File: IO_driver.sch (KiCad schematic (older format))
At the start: 9 parts, among them J2001 BNC, U2001 74LVC2T45DC

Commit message: some fixes; don't recall details :-(
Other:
- moved on the sheet: R2052
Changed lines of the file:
@@
 $Descr A4 11693 8268
 encoding utf-8
-Sheet 11 12
+Sheet 10 12
 Title ""
 Date ""
@@
 	3850 1850 4050 1850
 Connection ~ 4050 1850
-Text HLabel 3250 1850 0    50   BiDi ~ 0
+Text HLabel 2500 1850 0    50   BiDi ~ 0
 DATA
-Wire Wire Line
-	3250 1850 3500 1850
-Text HLabel 3250 2150 0    50   Input ~ 0
+Text HLabel 2500 2150 0    50   Input ~ 0
 DIR
-Wire Wire Line
-	3250 2150 3600 2150
 $Comp
 L Device:C_Small C2001
@@
 L Device:R_Small R?
 U 1 1 60E4921E
-P 3600 2350
+P 3500 2350
 AR Path="/60DC28BD/60E4921E" Ref="R?"  Part="1"
 AR Path="/60E4921E" Ref="R?"  Part="1"
@@
 AR Path="/60E70F2C/60EF9F81/60E4921E" Ref="R2002"  Part="1"
 AR Path="/60E70F2C/60E556C7/60E4921E" Ref="R2052"  Part="1"
-F 0 "R2052" H 3659 2396 50  0000 L CNN
-F 1 "2k2" H 3659 2305 50  0000 L CNN
-F 2 "Resistor_SMD:R_0603_1608Metric" H 3600 2350 50  0001 C CNN
-F 3 "~" H 3600 2350 50  0001 C CNN
-	1    3600 2350
-	1    0    0    -1
-$EndComp
-Wire Wire Line
-	3600 2250 3600 2150
-Connection ~ 3600 2150
-Wire Wire Line
-	3600 2150 4100 2150
-Wire Wire Line
-	3600 2450 3600 2550
-Wire Wire Line
-	3600 2550 4500 2550
+F 0 "R2052" H 3559 2396 50  0000 L CNN
+F 1 "2k2" H 3559 2305 50  0000 L CNN
+F 2 "Resistor_SMD:R_0603_1608Metric" H 3500 2350 50  0001 C CNN
+F 3 "~" H 3500 2350 50  0001 C CNN
+	1    3500 2350
+	1    0    0    -1
+$EndComp
 Connection ~ 4500 2550
 Wire Wire Line
@@
 Wire Wire Line
 	3500 1600 3500 1850
-Connection ~ 3500 1850
 Wire Wire Line
 	3500 1850 3650 1850
@@
 Wire Wire Line
 	4400 1300 4400 1350
+Wire Wire Line
+	3500 2150 3500 2250
+Wire Wire Line
+	3500 2150 4100 2150
+Wire Wire Line
+	3500 2450 3500 2550
+Wire Wire Line
+	3500 2550 4500 2550
+Wire Wire Line
+	2500 2150 3500 2150
+Connection ~ 3500 2150
+Wire Wire Line
+	2500 1850 3500 1850
+Connection ~ 3500 1850
 $EndSCHEMATC

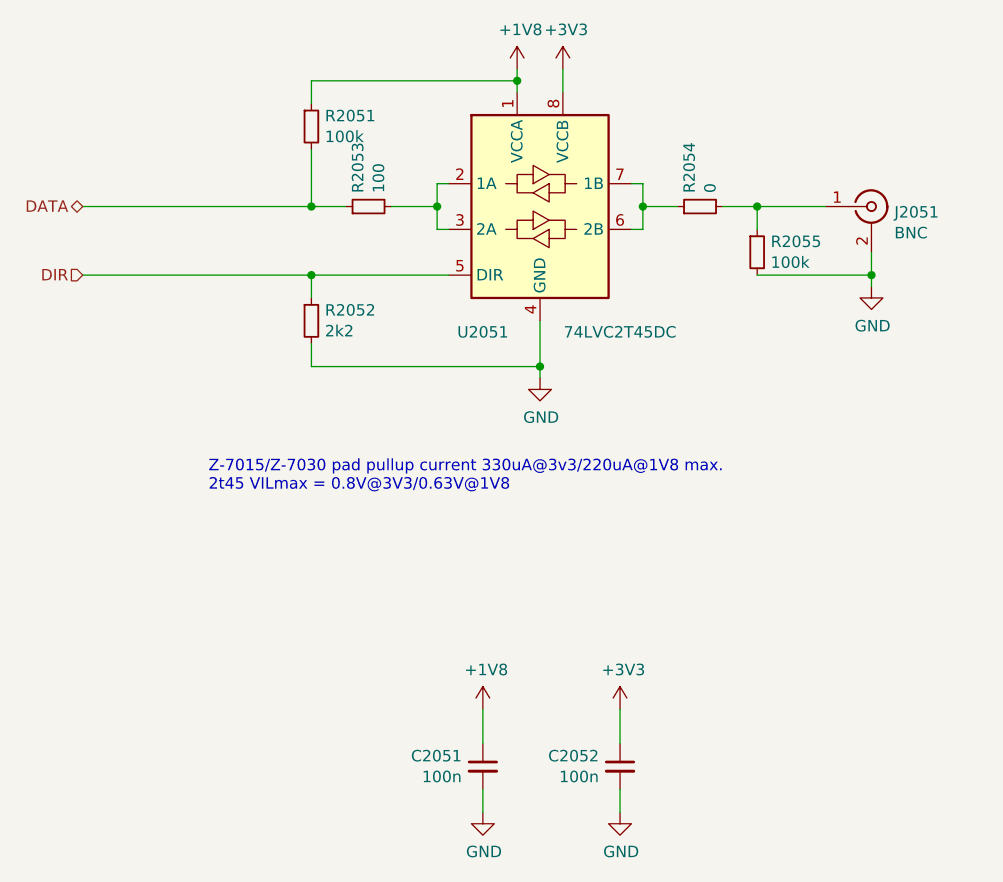
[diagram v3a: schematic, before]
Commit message: changed LED drivers; added Jumpers, write-protect
Modified LED drivers (XOR approach) to work with lan9254's
open-drain/-source outputs.

Routed spare switches as jumpers out of this module.

Route eeprom-write protect out of this module.
Route eeprom-isolation switch info out (so that FPGA may easily
determine whether EEPROM emulation is used or not).
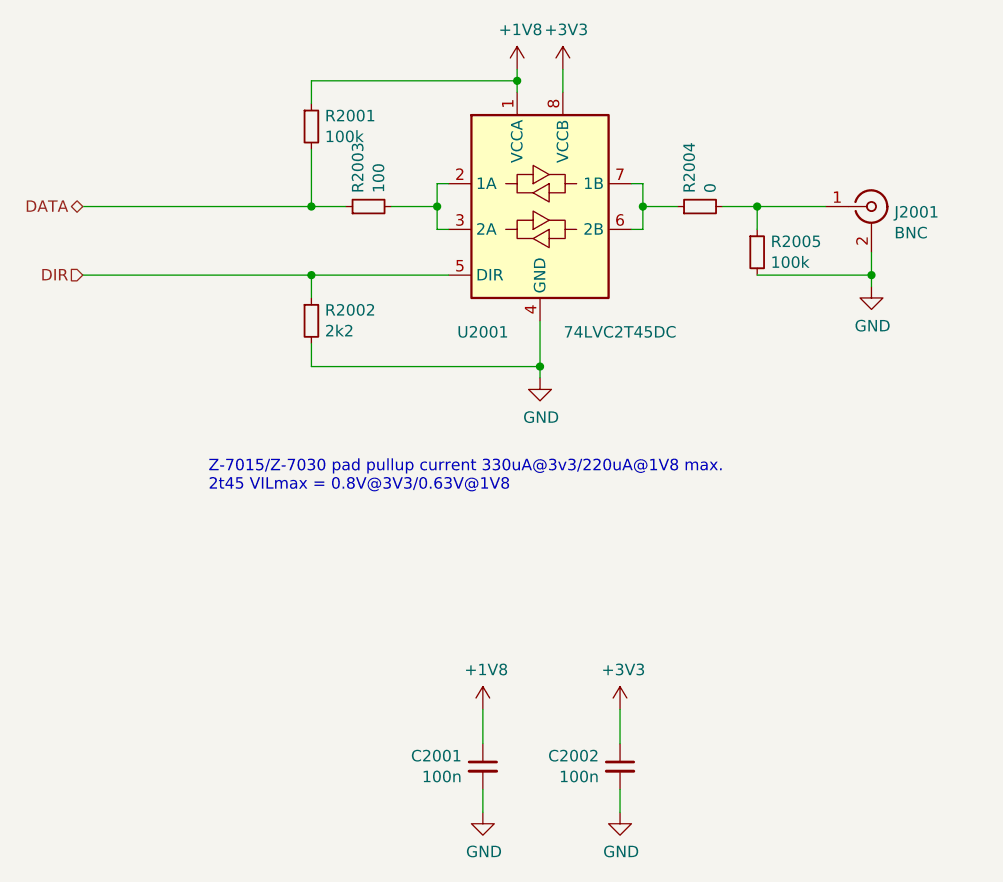
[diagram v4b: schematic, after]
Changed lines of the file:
@@
 $Descr A4 11693 8268
 encoding utf-8
-Sheet 10 18
+Sheet 16 18
 Title ""
 Date ""
@@
 AR Path="/60E70F2C/60EF9F81/60F26603" Ref="R2004"  Part="1"
 AR Path="/60E70F2C/60E556C7/60F26603" Ref="R2054"  Part="1"
-F 0 "R2054" H 5259 1896 50  0000 L CNN
+F 0 "R2004" H 5259 1896 50  0000 L CNN
 F 1 "0" H 5259 1805 50  0000 L CNN
 F 2 "Resistor_SMD:R_0603_1608Metric" H 5200 1850 50  0001 C CNN
@@
 AR Path="/60E70F2C/60EF9F81/60F26C82" Ref="R2003"  Part="1"
 AR Path="/60E70F2C/60E556C7/60F26C82" Ref="R2053"  Part="1"
-F 0 "R2053" H 3809 1896 50  0000 L CNN
+F 0 "R2003" H 3809 1896 50  0000 L CNN
 F 1 "100" H 3809 1805 50  0000 L CNN
 F 2 "Resistor_SMD:R_0603_1608Metric" H 3750 1850 50  0001 C CNN
@@
 AR Path="/60E70F2C/60EF9F81/60F2A5CB" Ref="C2001"  Part="1"
 AR Path="/60E70F2C/60E556C7/60F2A5CB" Ref="C2051"  Part="1"
-F 0 "C2051" H 4342 4346 50  0000 L CNN
+F 0 "C2001" H 4342 4346 50  0000 L CNN
 F 1 "100n" H 4342 4255 50  0000 L CNN
 F 2 "Capacitor_SMD:C_0402_1005Metric" H 4250 4300 50  0001 C CNN
@@
 AR Path="/60E70F2C/60EF9F81/60F2C544" Ref="C2002"  Part="1"
 AR Path="/60E70F2C/60E556C7/60F2C544" Ref="C2052"  Part="1"
-F 0 "C2052" H 4942 4346 50  0000 L CNN
+F 0 "C2002" H 4942 4346 50  0000 L CNN
 F 1 "100n" H 4942 4255 50  0000 L CNN
 F 2 "Capacitor_SMD:C_0402_1005Metric" H 4850 4300 50  0001 C CNN
@@
 AR Path="/60E70F2C/60EF9F81/60E51E93" Ref="J2001"  Part="1"
 AR Path="/60E70F2C/60E556C7/60E51E93" Ref="J2051"  Part="1"
-F 0 "J2051" H 6050 1825 50  0000 L CNN
+F 0 "J2001" H 6050 1825 50  0000 L CNN
 F 1 "BNC" H 6050 1734 50  0000 L CNN
 F 2 "proj_footprints:BNC_Molex_0731713150" H 5950 1850 50  0001 C CNN
@@
 AR Path="/60E70F2C/60EF9F81/60F05839" Ref="R2005"  Part="1"
 AR Path="/60E70F2C/60E556C7/60F05839" Ref="R2055"  Part="1"
-F 0 "R2055" H 5509 2096 50  0000 L CNN
+F 0 "R2005" H 5509 2096 50  0000 L CNN
 F 1 "100k" H 5509 2005 50  0000 L CNN
 F 2 "Resistor_SMD:R_0603_1608Metric" H 5450 2050 50  0001 C CNN
@@
 AR Path="/60E70F2C/60EF9F81/60E41AAA" Ref="U2001"  Part="1"
 AR Path="/60E70F2C/60E556C7/60E41AAA" Ref="U2051"  Part="1"
-F 0 "U2051" H 4250 1300 50  0000 C CNN
+F 0 "U2001" H 4250 1300 50  0000 C CNN
 F 1 "74LVC2T45DC" H 4850 1300 50  0000 C CNN
 F 2 "Package_SO:VSSOP-8_2.3x2mm_P0.5mm" H 4500 1000 50  0001 C CNN
@@
 AR Path="/60E70F2C/60EF9F81/60E4921E" Ref="R2002"  Part="1"
 AR Path="/60E70F2C/60E556C7/60E4921E" Ref="R2052"  Part="1"
-F 0 "R2052" H 3559 2396 50  0000 L CNN
+F 0 "R2002" H 3559 2396 50  0000 L CNN
 F 1 "2k2" H 3559 2305 50  0000 L CNN
 F 2 "Resistor_SMD:R_0603_1608Metric" H 3500 2350 50  0001 C CNN
@@
 AR Path="/60E70F2C/60EF9F81/60E49E8E" Ref="R2001"  Part="1"
 AR Path="/60E70F2C/60E556C7/60E49E8E" Ref="R2051"  Part="1"
-F 0 "R2051" H 3559 1546 50  0000 L CNN
+F 0 "R2001" H 3559 1546 50  0000 L CNN
 F 1 "100k" H 3559 1455 50  0000 L CNN
 F 2 "Resistor_SMD:R_0603_1608Metric" H 3500 1500 50  0001 C CNN

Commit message: further work...
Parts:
- J2001: footprint proj_footprints:BNC_Molex_0731713150 -> proj_footprints:LEMO+SMA
- R2002: value 2k2 -> 3k3
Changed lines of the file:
@@
 $Descr A4 11693 8268
 encoding utf-8
-Sheet 16 18
+Sheet 16 20
 Title ""
 Date ""
@@
 AR Path="/60E70F2C/60EF9F81/60F24852" Ref="#PWR?"  Part="1"
 AR Path="/60E70F2C/60E556C7/60F24852" Ref="#PWR?"  Part="1"
+AR Path="/60E70F2C/626DBAF0/60F24852" Ref="#PWR?"  Part="1"
 F 0 "#PWR?" H 4400 1100 50  0001 C CNN
 F 1 "+1V8" H 4415 1423 50  0000 C CNN
@@
 AR Path="/60E70F2C/60EF9F81/60F24858" Ref="#PWR?"  Part="1"
 AR Path="/60E70F2C/60E556C7/60F24858" Ref="#PWR?"  Part="1"
+AR Path="/60E70F2C/626DBAF0/60F24858" Ref="#PWR?"  Part="1"
 F 0 "#PWR?" H 4500 2350 50  0001 C CNN
 F 1 "GND" H 4505 2427 50  0000 C CNN
@@
 AR Path="/60E70F2C/60EF9F81/60F2485E" Ref="#PWR?"  Part="1"
 AR Path="/60E70F2C/60E556C7/60F2485E" Ref="#PWR?"  Part="1"
+AR Path="/60E70F2C/626DBAF0/60F2485E" Ref="#PWR?"  Part="1"
 F 0 "#PWR?" H 4600 1100 50  0001 C CNN
 F 1 "+3V3" H 4615 1423 50  0000 C CNN
@@
 AR Path="/60E70F2C/60EF9F81/60F26603" Ref="R2004"  Part="1"
 AR Path="/60E70F2C/60E556C7/60F26603" Ref="R2054"  Part="1"
-F 0 "R2004" H 5259 1896 50  0000 L CNN
+AR Path="/60E70F2C/626DBAF0/60F26603" Ref="R94"  Part="1"
+F 0 "R2054" H 5259 1896 50  0000 L CNN
 F 1 "0" H 5259 1805 50  0000 L CNN
 F 2 "Resistor_SMD:R_0603_1608Metric" H 5200 1850 50  0001 C CNN
@@
 AR Path="/60E70F2C/60EF9F81/60F26C82" Ref="R2003"  Part="1"
 AR Path="/60E70F2C/60E556C7/60F26C82" Ref="R2053"  Part="1"
-F 0 "R2003" H 3809 1896 50  0000 L CNN
+AR Path="/60E70F2C/626DBAF0/60F26C82" Ref="R93"  Part="1"
+F 0 "R2053" H 3809 1896 50  0000 L CNN
 F 1 "100" H 3809 1805 50  0000 L CNN
 F 2 "Resistor_SMD:R_0603_1608Metric" H 3750 1850 50  0001 C CNN
@@
 AR Path="/60E70F2C/60EF9F81/60F2A5CB" Ref="C2001"  Part="1"
 AR Path="/60E70F2C/60E556C7/60F2A5CB" Ref="C2051"  Part="1"
-F 0 "C2001" H 4342 4346 50  0000 L CNN
+AR Path="/60E70F2C/626DBAF0/60F2A5CB" Ref="C106"  Part="1"
+F 0 "C2051" H 4342 4346 50  0000 L CNN
 F 1 "100n" H 4342 4255 50  0000 L CNN
 F 2 "Capacitor_SMD:C_0402_1005Metric" H 4250 4300 50  0001 C CNN
@@
 AR Path="/60E70F2C/60EF9F81/60F2A810" Ref="#PWR?"  Part="1"
 AR Path="/60E70F2C/60E556C7/60F2A810" Ref="#PWR?"  Part="1"
+AR Path="/60E70F2C/626DBAF0/60F2A810" Ref="#PWR?"  Part="1"
 F 0 "#PWR?" H 4250 4250 50  0001 C CNN
 F 1 "GND" H 4255 4327 50  0000 C CNN
@@
 AR Path="/60E70F2C/60EF9F81/60F2AAF6" Ref="#PWR?"  Part="1"
 AR Path="/60E70F2C/60E556C7/60F2AAF6" Ref="#PWR?"  Part="1"
+AR Path="/60E70F2C/626DBAF0/60F2AAF6" Ref="#PWR?"  Part="1"
 F 0 "#PWR?" H 4250 3900 50  0001 C CNN
 F 1 "+1V8" H 4265 4223 50  0000 C CNN
@@
 AR Path="/60E70F2C/60EF9F81/60F2C544" Ref="C2002"  Part="1"
 AR Path="/60E70F2C/60E556C7/60F2C544" Ref="C2052"  Part="1"
-F 0 "C2002" H 4942 4346 50  0000 L CNN
+AR Path="/60E70F2C/626DBAF0/60F2C544" Ref="C107"  Part="1"
+F 0 "C2052" H 4942 4346 50  0000 L CNN
 F 1 "100n" H 4942 4255 50  0000 L CNN
 F 2 "Capacitor_SMD:C_0402_1005Metric" H 4850 4300 50  0001 C CNN
@@
 AR Path="/60E70F2C/60EF9F81/60F2C5F6" Ref="#PWR?"  Part="1"
 AR Path="/60E70F2C/60E556C7/60F2C5F6" Ref="#PWR?"  Part="1"
+AR Path="/60E70F2C/626DBAF0/60F2C5F6" Ref="#PWR?"  Part="1"
 F 0 "#PWR?" H 4850 4250 50  0001 C CNN
 F 1 "GND" H 4855 4327 50  0000 C CNN
@@
 AR Path="/60E70F2C/60EF9F81/60F2D29B" Ref="#PWR?"  Part="1"
 AR Path="/60E70F2C/60E556C7/60F2D29B" Ref="#PWR?"  Part="1"
+AR Path="/60E70F2C/626DBAF0/60F2D29B" Ref="#PWR?"  Part="1"
 F 0 "#PWR?" H 4850 3900 50  0001 C CNN
 F 1 "+3V3" H 4865 4223 50  0000 C CNN
@@
 AR Path="/60E70F2C/60EF9F81/60E51E93" Ref="J2001"  Part="1"
 AR Path="/60E70F2C/60E556C7/60E51E93" Ref="J2051"  Part="1"
-F 0 "J2001" H 6050 1825 50  0000 L CNN
+AR Path="/60E70F2C/626DBAF0/60E51E93" Ref="J5"  Part="1"
+F 0 "J2051" H 6050 1825 50  0000 L CNN
 F 1 "BNC" H 6050 1734 50  0000 L CNN
-F 2 "proj_footprints:BNC_Molex_0731713150" H 5950 1850 50  0001 C CNN
+F 2 "proj_footprints:LEMO+SMA" H 5950 1850 50  0001 C CNN
 F 3 " ~" H 5950 1850 50  0001 C CNN
 F 4 "0731713150" H 5950 1850 50  0001 C CNN "Part"
@@
 AR Path="/60E70F2C/60EF9F81/60E52CD9" Ref="#PWR?"  Part="1"
 AR Path="/60E70F2C/60E556C7/60E52CD9" Ref="#PWR?"  Part="1"
+AR Path="/60E70F2C/626DBAF0/60E52CD9" Ref="#PWR?"  Part="1"
 F 0 "#PWR?" H 5950 1950 50  0001 C CNN
 F 1 "GND" H 5955 2027 50  0000 C CNN
@@
 AR Path="/60E70F2C/60EF9F81/60F05839" Ref="R2005"  Part="1"
 AR Path="/60E70F2C/60E556C7/60F05839" Ref="R2055"  Part="1"
-F 0 "R2005" H 5509 2096 50  0000 L CNN
+AR Path="/60E70F2C/626DBAF0/60F05839" Ref="R95"  Part="1"
+F 0 "R2055" H 5509 2096 50  0000 L CNN
 F 1 "100k" H 5509 2005 50  0000 L CNN
 F 2 "Resistor_SMD:R_0603_1608Metric" H 5450 2050 50  0001 C CNN
@@
 AR Path="/60E70F2C/60EF9F81/60E41AAA" Ref="U2001"  Part="1"
 AR Path="/60E70F2C/60E556C7/60E41AAA" Ref="U2051"  Part="1"
-F 0 "U2001" H 4250 1300 50  0000 C CNN
+AR Path="/60E70F2C/626DBAF0/60E41AAA" Ref="U22"  Part="1"
+F 0 "U2051" H 4250 1300 50  0000 C CNN
 F 1 "74LVC2T45DC" H 4850 1300 50  0000 C CNN
 F 2 "Package_SO:VSSOP-8_2.3x2mm_P0.5mm" H 4500 1000 50  0001 C CNN
@@
 AR Path="/60E70F2C/60EF9F81/60E4921E" Ref="R2002"  Part="1"
 AR Path="/60E70F2C/60E556C7/60E4921E" Ref="R2052"  Part="1"
-F 0 "R2002" H 3559 2396 50  0000 L CNN
-F 1 "2k2" H 3559 2305 50  0000 L CNN
+AR Path="/60E70F2C/626DBAF0/60E4921E" Ref="R92"  Part="1"
+F 0 "R2052" H 3559 2396 50  0000 L CNN
+F 1 "3k3" H 3559 2305 50  0000 L CNN
 F 2 "Resistor_SMD:R_0603_1608Metric" H 3500 2350 50  0001 C CNN
 F 3 "~" H 3500 2350 50  0001 C CNN
@@
 AR Path="/60E70F2C/60EF9F81/60E49E8E" Ref="R2001"  Part="1"
 AR Path="/60E70F2C/60E556C7/60E49E8E" Ref="R2051"  Part="1"
-F 0 "R2001" H 3559 1546 50  0000 L CNN
+AR Path="/60E70F2C/626DBAF0/60E49E8E" Ref="R91"  Part="1"
+F 0 "R2051" H 3559 1546 50  0000 L CNN
 F 1 "100k" H 3559 1455 50  0000 L CNN
 F 2 "Resistor_SMD:R_0603_1608Metric" H 3500 1500 50  0001 C CNN

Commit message: added 3rd GPIO
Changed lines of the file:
@@
 $Descr A4 11693 8268
 encoding utf-8
-Sheet 16 20
+Sheet 18 21
 Title ""
 Date ""
@@
 AR Path="/60E70F2C/60E556C7/60F24852" Ref="#PWR?"  Part="1"
 AR Path="/60E70F2C/626DBAF0/60F24852" Ref="#PWR?"  Part="1"
+AR Path="/60E70F2C/62739E15/60F24852" Ref="#PWR?"  Part="1"
 F 0 "#PWR?" H 4400 1100 50  0001 C CNN
 F 1 "+1V8" H 4415 1423 50  0000 C CNN
@@
 AR Path="/60E70F2C/60E556C7/60F24858" Ref="#PWR?"  Part="1"
 AR Path="/60E70F2C/626DBAF0/60F24858" Ref="#PWR?"  Part="1"
+AR Path="/60E70F2C/62739E15/60F24858" Ref="#PWR?"  Part="1"
 F 0 "#PWR?" H 4500 2350 50  0001 C CNN
 F 1 "GND" H 4505 2427 50  0000 C CNN
@@
 AR Path="/60E70F2C/60E556C7/60F2485E" Ref="#PWR?"  Part="1"
 AR Path="/60E70F2C/626DBAF0/60F2485E" Ref="#PWR?"  Part="1"
+AR Path="/60E70F2C/62739E15/60F2485E" Ref="#PWR?"  Part="1"
 F 0 "#PWR?" H 4600 1100 50  0001 C CNN
 F 1 "+3V3" H 4615 1423 50  0000 C CNN
@@
 AR Path="/60E70F2C/60E556C7/60F26603" Ref="R2054"  Part="1"
 AR Path="/60E70F2C/626DBAF0/60F26603" Ref="R94"  Part="1"
-F 0 "R2054" H 5259 1896 50  0000 L CNN
+AR Path="/60E70F2C/62739E15/60F26603" Ref="R2009"  Part="1"
+F 0 "R2009" H 5259 1896 50  0000 L CNN
 F 1 "0" H 5259 1805 50  0000 L CNN
 F 2 "Resistor_SMD:R_0603_1608Metric" H 5200 1850 50  0001 C CNN
@@
 AR Path="/60E70F2C/60E556C7/60F26C82" Ref="R2053"  Part="1"
 AR Path="/60E70F2C/626DBAF0/60F26C82" Ref="R93"  Part="1"
-F 0 "R2053" H 3809 1896 50  0000 L CNN
+AR Path="/60E70F2C/62739E15/60F26C82" Ref="R2008"  Part="1"
+F 0 "R2008" H 3809 1896 50  0000 L CNN
 F 1 "100" H 3809 1805 50  0000 L CNN
 F 2 "Resistor_SMD:R_0603_1608Metric" H 3750 1850 50  0001 C CNN
@@
 AR Path="/60E70F2C/60E556C7/60F2A5CB" Ref="C2051"  Part="1"
 AR Path="/60E70F2C/626DBAF0/60F2A5CB" Ref="C106"  Part="1"
-F 0 "C2051" H 4342 4346 50  0000 L CNN
+AR Path="/60E70F2C/62739E15/60F2A5CB" Ref="C2003"  Part="1"
+F 0 "C2003" H 4342 4346 50  0000 L CNN
 F 1 "100n" H 4342 4255 50  0000 L CNN
 F 2 "Capacitor_SMD:C_0402_1005Metric" H 4250 4300 50  0001 C CNN
@@
 AR Path="/60E70F2C/60E556C7/60F2A810" Ref="#PWR?"  Part="1"
 AR Path="/60E70F2C/626DBAF0/60F2A810" Ref="#PWR?"  Part="1"
+AR Path="/60E70F2C/62739E15/60F2A810" Ref="#PWR?"  Part="1"
 F 0 "#PWR?" H 4250 4250 50  0001 C CNN
 F 1 "GND" H 4255 4327 50  0000 C CNN
@@
 AR Path="/60E70F2C/60E556C7/60F2AAF6" Ref="#PWR?"  Part="1"
 AR Path="/60E70F2C/626DBAF0/60F2AAF6" Ref="#PWR?"  Part="1"
+AR Path="/60E70F2C/62739E15/60F2AAF6" Ref="#PWR?"  Part="1"
 F 0 "#PWR?" H 4250 3900 50  0001 C CNN
 F 1 "+1V8" H 4265 4223 50  0000 C CNN
@@
 AR Path="/60E70F2C/60E556C7/60F2C544" Ref="C2052"  Part="1"
 AR Path="/60E70F2C/626DBAF0/60F2C544" Ref="C107"  Part="1"
-F 0 "C2052" H 4942 4346 50  0000 L CNN
+AR Path="/60E70F2C/62739E15/60F2C544" Ref="C2004"  Part="1"
+F 0 "C2004" H 4942 4346 50  0000 L CNN
 F 1 "100n" H 4942 4255 50  0000 L CNN
 F 2 "Capacitor_SMD:C_0402_1005Metric" H 4850 4300 50  0001 C CNN
@@
 AR Path="/60E70F2C/60E556C7/60F2C5F6" Ref="#PWR?"  Part="1"
 AR Path="/60E70F2C/626DBAF0/60F2C5F6" Ref="#PWR?"  Part="1"
+AR Path="/60E70F2C/62739E15/60F2C5F6" Ref="#PWR?"  Part="1"
 F 0 "#PWR?" H 4850 4250 50  0001 C CNN
 F 1 "GND" H 4855 4327 50  0000 C CNN
@@
 AR Path="/60E70F2C/60E556C7/60F2D29B" Ref="#PWR?"  Part="1"
 AR Path="/60E70F2C/626DBAF0/60F2D29B" Ref="#PWR?"  Part="1"
+AR Path="/60E70F2C/62739E15/60F2D29B" Ref="#PWR?"  Part="1"
 F 0 "#PWR?" H 4850 3900 50  0001 C CNN
 F 1 "+3V3" H 4865 4223 50  0000 C CNN
@@
 AR Path="/60E70F2C/60E556C7/60E51E93" Ref="J2051"  Part="1"
 AR Path="/60E70F2C/626DBAF0/60E51E93" Ref="J5"  Part="1"
-F 0 "J2051" H 6050 1825 50  0000 L CNN
+AR Path="/60E70F2C/62739E15/60E51E93" Ref="J2002"  Part="1"
+F 0 "J2002" H 6050 1825 50  0000 L CNN
 F 1 "BNC" H 6050 1734 50  0000 L CNN
 F 2 "proj_footprints:LEMO+SMA" H 5950 1850 50  0001 C CNN
@@
 AR Path="/60E70F2C/60E556C7/60E52CD9" Ref="#PWR?"  Part="1"
 AR Path="/60E70F2C/626DBAF0/60E52CD9" Ref="#PWR?"  Part="1"
+AR Path="/60E70F2C/62739E15/60E52CD9" Ref="#PWR?"  Part="1"
 F 0 "#PWR?" H 5950 1950 50  0001 C CNN
 F 1 "GND" H 5955 2027 50  0000 C CNN
@@
 AR Path="/60E70F2C/60E556C7/60F05839" Ref="R2055"  Part="1"
 AR Path="/60E70F2C/626DBAF0/60F05839" Ref="R95"  Part="1"
-F 0 "R2055" H 5509 2096 50  0000 L CNN
+AR Path="/60E70F2C/62739E15/60F05839" Ref="R2010"  Part="1"
+F 0 "R2010" H 5509 2096 50  0000 L CNN
 F 1 "100k" H 5509 2005 50  0000 L CNN
 F 2 "Resistor_SMD:R_0603_1608Metric" H 5450 2050 50  0001 C CNN
@@
 AR Path="/60E70F2C/60E556C7/60E41AAA" Ref="U2051"  Part="1"
 AR Path="/60E70F2C/626DBAF0/60E41AAA" Ref="U22"  Part="1"
-F 0 "U2051" H 4250 1300 50  0000 C CNN
+AR Path="/60E70F2C/62739E15/60E41AAA" Ref="U2002"  Part="1"
+F 0 "U2002" H 4250 1300 50  0000 C CNN
 F 1 "74LVC2T45DC" H 4850 1300 50  0000 C CNN
 F 2 "Package_SO:VSSOP-8_2.3x2mm_P0.5mm" H 4500 1000 50  0001 C CNN
@@
 AR Path="/60E70F2C/60E556C7/60E4921E" Ref="R2052"  Part="1"
 AR Path="/60E70F2C/626DBAF0/60E4921E" Ref="R92"  Part="1"
-F 0 "R2052" H 3559 2396 50  0000 L CNN
+AR Path="/60E70F2C/62739E15/60E4921E" Ref="R2007"  Part="1"
+F 0 "R2007" H 3559 2396 50  0000 L CNN
 F 1 "3k3" H 3559 2305 50  0000 L CNN
 F 2 "Resistor_SMD:R_0603_1608Metric" H 3500 2350 50  0001 C CNN
@@
 AR Path="/60E70F2C/60E556C7/60E49E8E" Ref="R2051"  Part="1"
 AR Path="/60E70F2C/626DBAF0/60E49E8E" Ref="R91"  Part="1"
-F 0 "R2051" H 3559 1546 50  0000 L CNN
+AR Path="/60E70F2C/62739E15/60E49E8E" Ref="R2006"  Part="1"
+F 0 "R2006" H 3559 1546 50  0000 L CNN
 F 1 "100k" H 3559 1455 50  0000 L CNN
 F 2 "Resistor_SMD:R_0603_1608Metric" H 3500 1500 50  0001 C CNN
